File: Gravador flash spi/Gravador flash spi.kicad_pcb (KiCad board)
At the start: 2 copper layers, 10 parts, among them J1 Chip Select, J2 DIL-8, J3 SO-8

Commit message: Corrigindo pcb
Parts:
- moved J1 69.2 mm to (154.9, 82.0)
- moved J2 69.2 mm to (159.3, 95.0)
- moved R1 69.2 mm to (149.5, 75.4)
- moved R2 69.2 mm to (152.1, 75.4)
- moved R3 69.2 mm to (134.8, 75.4)
- moved R5 69.2 mm to (142.2, 75.4)
- moved R6 69.2 mm to (144.7, 75.4)
- moved A1 69.2 mm to (137.9, 116.3)
- moved J3 69.2 mm to (139.1, 88.8)
- moved R4 69.2 mm to (137.1, 75.4)
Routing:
- net 3.3V: track 62.0 -> 101.5 mm
- net SCK_L: track 95.1 -> 65.0 mm
- net MOSI_L: track 84.7 -> 58.9 mm
- net GND: track 0.00 -> 15.5 mm, vias 0 -> 6
- net MISO: track 48.6 -> 47.2 mm
- net CS_DIL-8: track 15.0 -> 16.0 mm
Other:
- net class Default: trace_width 0.4 -> 0.2
- board text added: "Bottom"

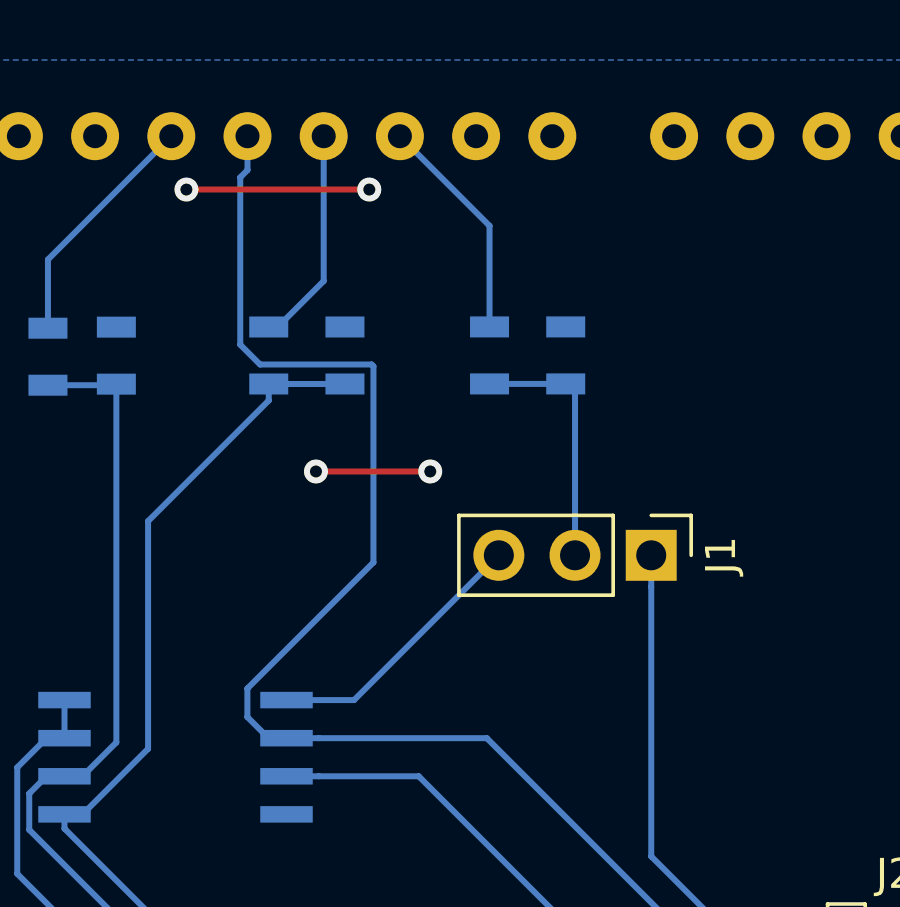
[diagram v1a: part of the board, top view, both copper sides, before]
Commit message: adicionando jumper de aterramento
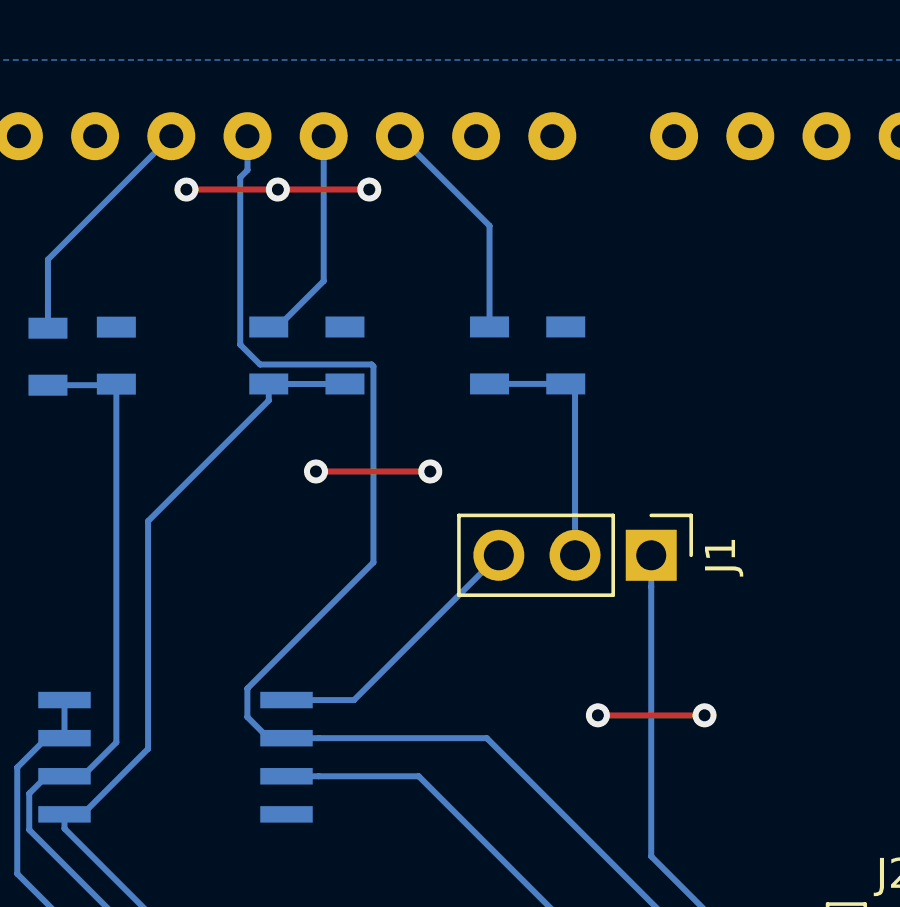
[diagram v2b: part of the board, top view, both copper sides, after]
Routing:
- net GND: track 15.5 -> 19.0 mm, vias 6 -> 9
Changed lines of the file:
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@@
     (thickness 1.6)
     (drawings 1)
-    (tracks 95)
+    (tracks 100)
     (zones 0)
     (modules 10)
@@
   (via (at 145.542 69.85) (size 0.8) (drill 0.4) (layers F.Cu B.Cu) (net 5))
   (via (at 139.446 69.85) (size 0.8) (drill 0.4) (layers F.Cu B.Cu) (net 5))
-  (segment (start 139.446 69.85) (end 145.542 69.85) (width 0.2) (layer F.Cu) (net 5))
   (via (at 151.384 103.378) (size 0.8) (drill 0.4) (layers F.Cu B.Cu) (net 5))
   (via (at 151.384 108.966) (size 0.8) (drill 0.4) (layers F.Cu B.Cu) (net 5))
   (segment (start 151.384 103.378) (end 151.384 108.966) (width 0.2) (layer F.Cu) (net 5))
+  (via (at 156.718 87.376) (size 0.8) (drill 0.4) (layers F.Cu B.Cu) (net 5))
+  (via (at 153.162 87.376) (size 0.8) (drill 0.4) (layers F.Cu B.Cu) (net 5))
+  (segment (start 156.718 87.376) (end 153.162 87.376) (width 0.2) (layer F.Cu) (net 5))
+  (via (at 142.494 69.85) (size 0.8) (drill 0.4) (layers F.Cu B.Cu) (net 5))
+  (segment (start 145.542 69.85) (end 142.494 69.85) (width 0.2) (layer F.Cu) (net 5))
+  (segment (start 139.446 69.85) (end 142.494 69.85) (width 0.2) (layer F.Cu) (net 5))
   (segment (start 166.878 100.076) (end 167.278 100.076) (width 0.4) (layer B.Cu) (net 6))
   (segment (start 137.075597 76.371859) (end 137.110596 76.33686) (width 0.2) (layer B.Cu) (net 6))
